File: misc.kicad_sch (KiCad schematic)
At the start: 44 parts, among them J2 Tag-Connect_TC2030-IDC-NL_2x3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, U1 MPFS250T-FCVG484, U2 SDINBDG4-8G, U3 MT25QL01GBBB1EW9-0SIT

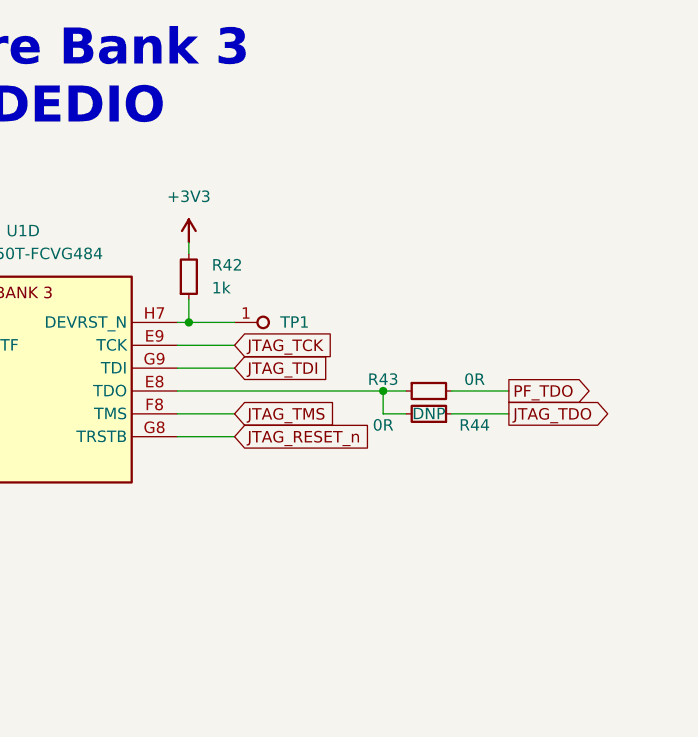
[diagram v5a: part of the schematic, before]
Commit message: [#54899] Flag not connected pins
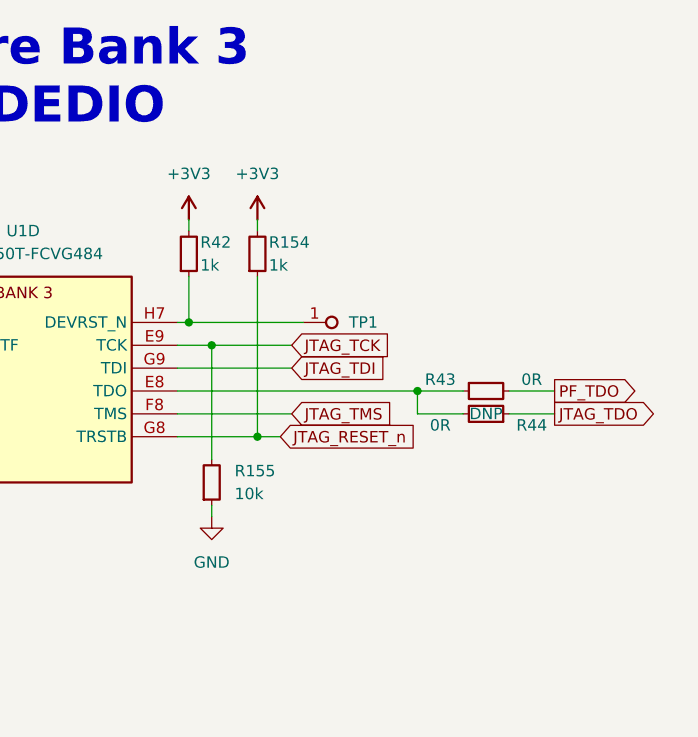
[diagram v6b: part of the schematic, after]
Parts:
- added R154: R_1k_0402, antmicro-footprints:R_0402_1005Metric, symbol antmicroResistors0402:R_1k_0402
- added R155: R_10k_0402, antmicro-footprints:R_0402_1005Metric, symbol antmicroResistors0402:R_10k_0402
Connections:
- net +3V3: now also R154.2
- net GND: now also R155.1
- net JTAG_RESET_n: now also R154.1
- net JTAG_TCK: now also R155.2
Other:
- moved on the sheet: R42, R43, R44, TP1

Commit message: [#54899] Update symbols
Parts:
- R25, R26, R27, R44: now in the parts list
- U1: footprint antmicro-footprints:BGA-484_19x19mm_Layout22x22_P0.8mm_FCVG484 -> antmicro-footprints:BGA-484_19x19mm_Layout22x22_P0.8mm_MPFS250T-FCVG484
- U3: value MT25QL01GBBB1EW9-0SIT -> MT25QL01GBBB1EW9-0SIT; symbol antmicroMemory:MT25QL01GBBB1EW9-0SIT -> antmicroMemory:MT25QL01GBBB1EW9-0SIT; MPN MT25QL01GBBB1EW9-0SIT -> MT25QL01GBBB1EW9-0SIT
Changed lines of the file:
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@@
   )
   (symbol (lib_id "antmicroResistorNetworksArrays:R_4x0R_0201_array") (at 138.43 66.04 0) (unit 1)
-    (in_bom no) (on_board yes) (dnp no)
+    (in_bom yes) (on_board yes) (dnp no)
     (property "Reference" "R25" (at 143.51 59.69 0)
       (effects (font (size 1.27 1.27) (thickness 0.15)))
@@
   )
   (symbol (lib_id "antmicroResistors0402:R_0R_0402") (at 388.62 85.09 180) (unit 1)
-    (in_bom no) (on_board yes) (dnp no)
+    (in_bom yes) (on_board yes) (dnp no)
     (property "Reference" "R44" (at 391.16 86.36 0)
       (effects (font (size 1.27 1.27) (thickness 0.15)))
@@
   )
   (symbol (lib_id "antmicroResistors0402:R_0R_0402") (at 140.97 96.52 0) (unit 1)
-    (in_bom no) (on_board yes) (dnp no)
+    (in_bom yes) (on_board yes) (dnp no)
     (property "Reference" "R27" (at 138.43 95.25 0)
       (effects (font (size 1.27 1.27) (thickness 0.15)))
@@
       (effects (font (size 1.27 1.27) (thickness 0.15)) (justify left bottom) hide)
     )
-    (property "Footprint" "antmicro-footprints:BGA-484_19x19mm_Layout22x22_P0.8mm_FCVG484" (at 157.48 208.28 0)
+    (property "Footprint" "antmicro-footprints:BGA-484_19x19mm_Layout22x22_P0.8mm_MPFS250T-FCVG484" (at 157.48 208.28 0)
       (effects (font (size 1.27 1.27) (thickness 0.15)) (justify left bottom) hide)
     )
@@
     )
   )
-  (symbol (lib_id "antmicroMemory:MT25QL01GBBB1EW9-0SIT ") (at 335.28 203.2 0) (unit 1)
+  (symbol (lib_id "antmicroMemory:MT25QL01GBBB1EW9-0SIT") (at 335.28 203.2 0) (unit 1)
     (in_bom yes) (on_board yes) (dnp no) (fields_autoplaced)
-    (property "Reference" "U3" (at 347.98 194.945 0)
-      (effects (font (size 1.27 1.27) (thickness 0.15)))
-    )
-    (property "Value" "MT25QL01GBBB1EW9-0SIT " (at 378.46 210.82 0)
+    (property "Reference" "U3" (at 347.98 195.58 0)
+      (effects (font (size 1.27 1.27) (thickness 0.15)))
+    )
+    (property "Value" "MT25QL01GBBB1EW9-0SIT" (at 378.46 210.82 0)
       (effects (font (size 1.27 1.27) (thickness 0.15)) (justify left bottom) hide)
     )
@@
       (effects (font (size 1.27 1.27) (thickness 0.15)) (justify left bottom) hide)
     )
-    (property "Datasheet" "https://www.mouser.pl/datasheet/2/671/mict_s_a0002234966_1-2290738.pdf" (at 378.46 215.9 0)
-      (effects (font (size 1.27 1.27) (thickness 0.15)) (justify left bottom) hide)
-    )
-    (property "MPN" "MT25QL01GBBB1EW9-0SIT " (at 347.98 197.485 0)
+    (property "Datasheet" "https://www.mouser.com/datasheet/2/671/mict_s_a0002234966_1-2290738.pdf" (at 378.46 215.9 0)
+      (effects (font (size 1.27 1.27) (thickness 0.15)) (justify left bottom) hide)
+    )
+    (property "MPN" "MT25QL01GBBB1EW9-0SIT" (at 347.98 198.12 0)
       (effects (font (size 1.27 1.27) (thickness 0.15)))
     )
@@
   )
   (symbol (lib_id "antmicroResistorNetworksArrays:R_4x0R_0201_array") (at 138.43 77.47 0) (unit 1)
-    (in_bom no) (on_board yes) (dnp no)
+    (in_bom yes) (on_board yes) (dnp no)
     (property "Reference" "R26" (at 143.51 87.63 0)
       (effects (font (size 1.27 1.27) (thickness 0.15)))
@@
       (effects (font (size 1.27 1.27) (thickness 0.15)) (justify left bottom) hide)
     )
-    (property "Footprint" "antmicro-footprints:BGA-484_19x19mm_Layout22x22_P0.8mm_FCVG484" (at 421.64 85.09 0)
-      (effects (font (size 1.27 1.27) (thickness 0.15)) (justify left bottom) hide)
-    )
+    (property "Footprint" "antmicro-footprints:BGA-484_19x19mm_Layout22x22_P0.8mm_MPFS250T-FCVG484" (at 421.64 85.09 0)
+      (effects (font (size 1.27 1.27) (thickness 0.15)) (justify left bottom) hide)
+    )

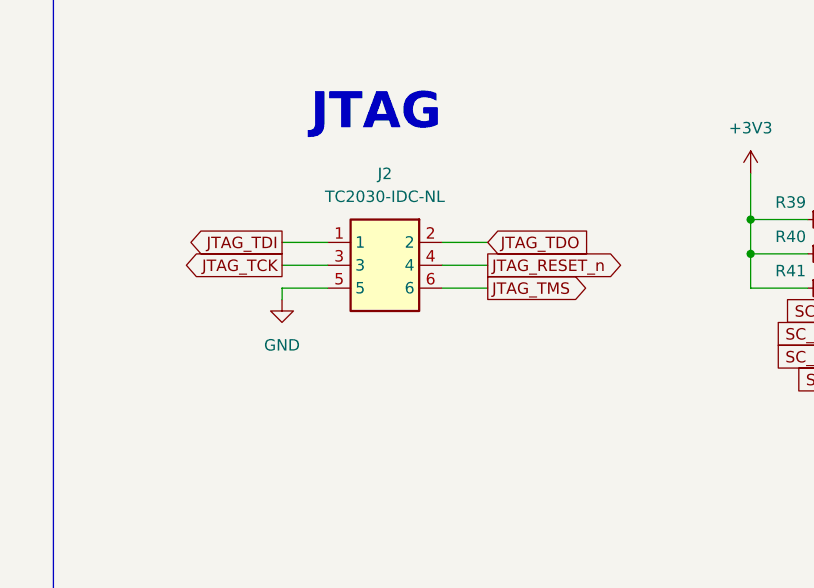
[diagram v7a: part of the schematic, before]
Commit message: [#55288] Replace Tag-Connect with test points
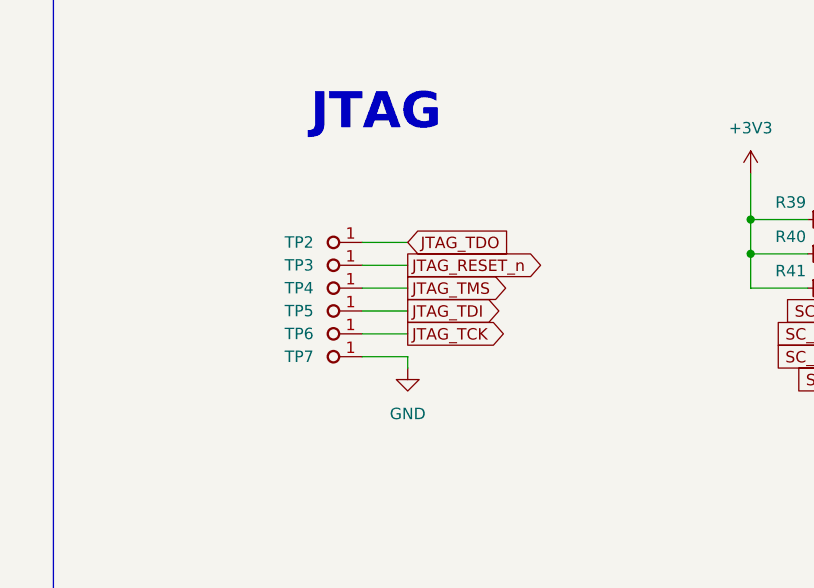
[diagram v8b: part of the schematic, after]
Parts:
- removed J2: Tag-Connect_TC2030-IDC-NL_2x3_P1.27mm, antmicro-footprints:Tag-Connect_TC2030-IDC-NL_2x3_P1.27mm, symbol antmicroTestPoints:Tag-Connect_TC2030-IDC-NL_2x3_P1.27mm
- added TP2, TP3, TP4, TP5, TP6, TP7: TP_0.75mm_SMD, antmicro-footprints:TP_SMD_0.75mm, symbol antmicroTestPoints:TP_0.75mm_SMD
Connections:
- net GND: now also TP7.1
- net JTAG_RESET_n: now also TP3.1
- net JTAG_TCK: now also TP6.1
- net JTAG_TDI: now also TP5.1
- net JTAG_TDO: now also TP2.1
- net JTAG_TMS: now also TP4.1
